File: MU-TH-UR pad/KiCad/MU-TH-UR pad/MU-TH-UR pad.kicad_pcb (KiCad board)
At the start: 2 copper layers, 186.4 x 62.5 mm, 43 parts, among them J1 OLED_DISPLAY, SW1 RotaryEncoder_Switch, SW2 SW_Push_45deg, SW3 SW_Push_45deg, SW4 SW_Push_45deg, SW5 SW_Push_45deg, U3 RP2040-Zero

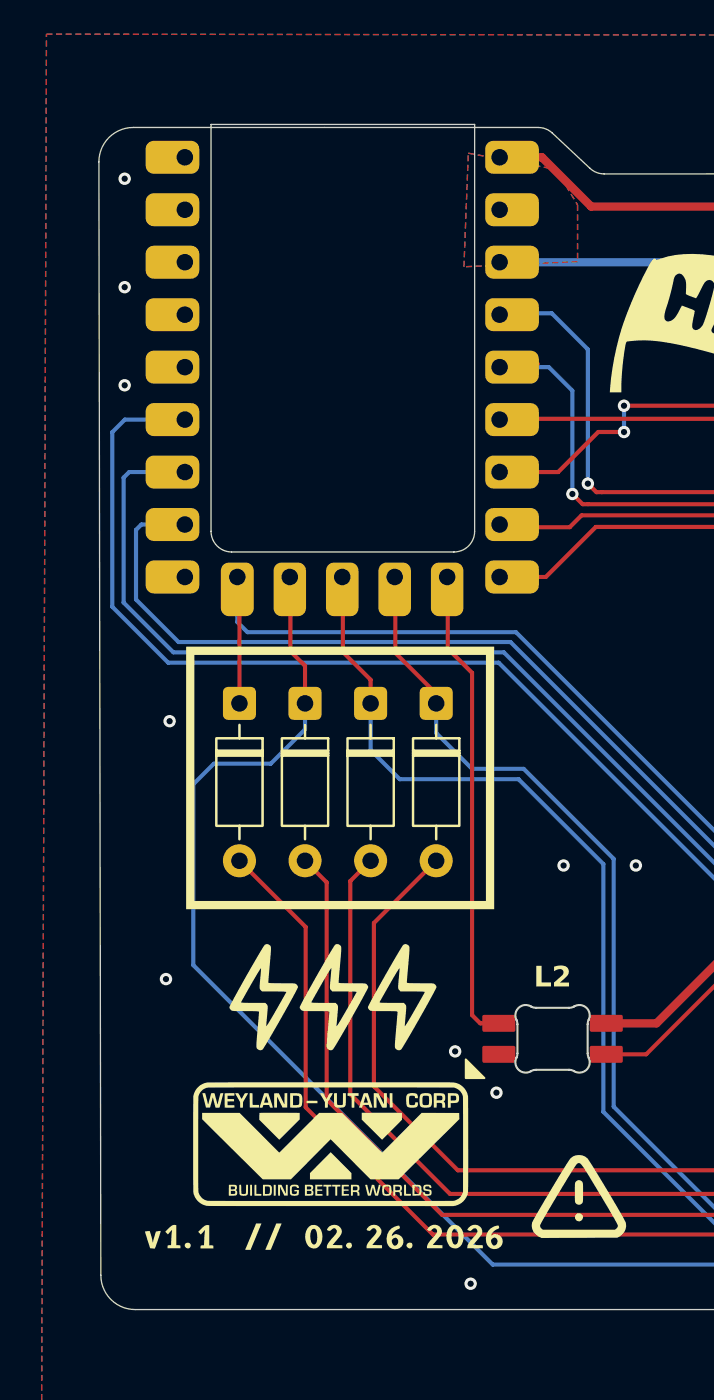
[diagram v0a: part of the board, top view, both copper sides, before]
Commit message: Fixed Edge Cut
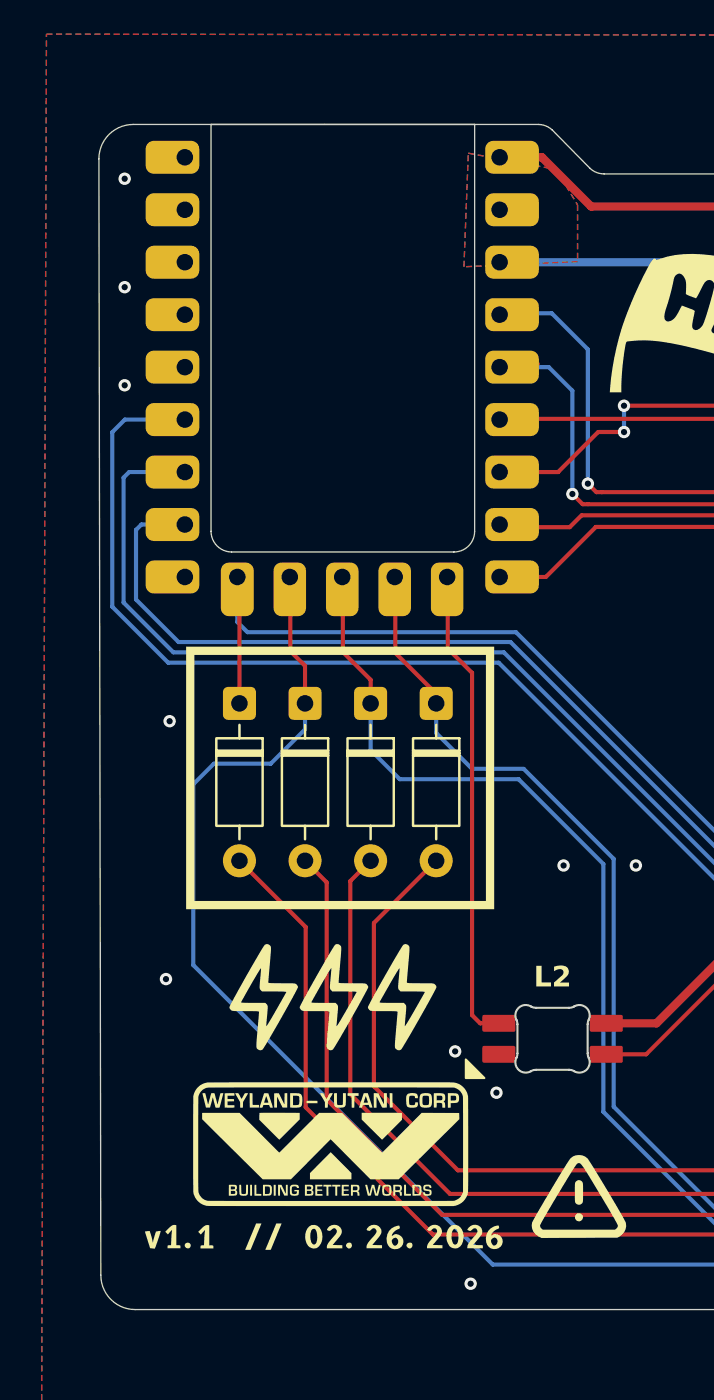
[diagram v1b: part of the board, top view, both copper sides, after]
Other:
- board size 186.4 x 62.5 mm -> 186.4 x 62.7 mm
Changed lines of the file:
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@@
 		(allow_soldermask_bridges_in_footprints no)
 		(tenting front back)
-		(grid_origin 105.626675 8.487754)
+		(grid_origin 59.631863 58.846281)
 		(pcbplotparams
 			(layerselection 0x00000000_00000000_55555555_5755f5ff)
@@
 	)
 	(gr_arc
-		(start 54.202507 60.655752)
-		(mid 54.689627 59.4797)
-		(end 55.865679 58.99258)
+		(start 54.202507 60.509453)
+		(mid 54.689627 59.333401)
+		(end 55.865679 58.846281)
 		(stroke
 			(width 0.05)
@@
 	)
 	(gr_arc
-		(start 75.470739 58.99258)
-		(mid 75.838096 59.0625)
-		(end 76.154082 59.262483)
+		(start 75.470739 58.846281)
+		(mid 75.838096 58.916201)
+		(end 76.154082 59.116184)
 		(stroke
 			(width 0.05)
@@
 	)
 	(gr_line
-		(start 76.154082 59.262483)
+		(start 76.154082 59.116213)
 		(end 77.98107 60.972474)
 		(stroke
@@
 	)
 	(gr_line
-		(start 55.865679 58.99258)
-		(end 65.115713 58.992579)
+		(start 55.865679 58.846281)
+		(end 65.115713 58.84628)
 		(stroke
 			(width 0.05)
@@
 	)
 	(gr_line
-		(start 75.470739 58.99258)
-		(end 65.115713 58.992579)
+		(start 75.470739 58.846282)
+		(end 65.115713 58.846281)
 		(stroke
 			(width 0.05)
@@
 	)
 	(gr_line
-		(start 54.202507 60.655752)
+		(start 54.202507 60.5094)
 		(end 54.296468 114.561714)
 		(stroke

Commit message: Added Serial Number Location for PCBWay
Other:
- board text added: "WayWayWay"
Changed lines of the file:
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@@
+		)
+	)
+	(gr_text "WayWayWay"
+		(at 60.881863 113.846281 0)
+		(layer "B.SilkS")
+		(effects
+			(font
+				(face "JetBrains Mono")
+				(size 1 1)
+				(thickness 0.25)
+				(bold yes)
+			)
+			(justify bottom mirror)
+		)
+		(render_cache "WayWayWay" 0
+			(polygon
+				(pts
+					(xy 64.532437 113.676281) (xy 64.638744 112.654979) (xy 64.493236 112.654979) (xy 64.428878 113.368473)
+					(xy 64.42265 113.46153) (xy 64.419109 113.557334) (xy 64.410011 113.46153) (xy 64.400913 113.368473)
+					(xy 64.311398 112.654979) (xy 64.161677 112.654979) (xy 64.077779 113.368473) (xy 64.067277 113.46153)
+					(xy 64.056774 113.557334) (xy 64.05189 113.46153) (xy 64.0456 113.368473) (xy 63.982647 112.654979)
+					(xy 63.838543 112.654979) (xy 63.950468 113.676281) (xy 64.143481 113.676281) (xy 64.221821 112.959977)
+					(xy 64.230248 112.861364) (xy 64.237209 112.765499) (xy 64.244231 112.861364) (xy 64.252657 112.959977)
+					(xy 64.337959 113.676281)
+				)
+			)
+			(polygon
+				(pts
+					(xy 63.46621 112.89735) (xy 63.525031 112.91011) (xy 63.574828 112.930177) (xy 63.617015 112.957168)
+					(xy 63.653541 112.99225) (xy 63.679792 113.031368) (xy 63.696716 113.075254) (xy 63.704393 113.125085)
+					(xy 63.536537 113.125085) (xy 63.530075 113.09812) (xy 63.51676 113.076075) (xy 63.495993 113.057919)
+					(xy 63.455506 113.040611) (xy 63.39799 113.034105) (xy 63.344983 113.039696) (xy 63.308249 113.05441)
+					(xy 63.283352 113.076786) (xy 63.267951 113.107721) (xy 63.262313 113.150242) (xy 63.262313 113.204831)
+					(xy 63.44977 113.204831) (xy 63.517072 113.209516) (xy 63.573567 113.222666) (xy 63.621071 113.243352)
+					(xy 63.66104 113.271265) (xy 63.694495 113.307049) (xy 63.718253 113.347945) (xy 63.73287 113.394972)
+					(xy 63.737976 113.449623) (xy 63.733441 113.50257) (xy 63.720459 113.548448) (xy 63.699453 113.588554)
+					(xy 63.670138 113.623829) (xy 63.634386 113.652097) (xy 63.592441 113.672718) (xy 63.543096 113.685677)
+					(xy 63.484758 113.690263) (xy 63.421602 113.685118) (xy 63.370125 113.670799) (xy 63.328076 113.648315)
+					(xy 63.293479 113.616629) (xy 63.270418 113.578439) (xy 63.2581 113.532177) (xy 63.2581 113.676281)
+					(xy 63.087436 113.676281) (xy 63.087436 113.409079) (xy 63.262313 113.409079) (xy 63.267485 113.448969)
+					(xy 63.282314 113.482003) (xy 63.307071 113.509829) (xy 63.338921 113.530071) (xy 63.378789 113.542924)
+					(xy 63.428826 113.547565) (xy 63.471557 113.54363) (xy 63.504653 113.532865) (xy 63.530248 113.516118)
+					(xy 63.549933 113.493063) (xy 63.561773 113.465742) (xy 63.565907 113.432831) (xy 63.562025 113.400686)
+					(xy 63.550865 113.37358) (xy 63.532324 113.350338) (xy 63.508141 113.332903) (xy 63.478358 113.322039)
+					(xy 63.441405 113.318159) (xy 63.262313 113.318159) (xy 63.262313 113.409079) (xy 63.087436 113.409079)
+					(xy 63.087436 113.154456) (xy 63.092956 113.093316) (xy 63.108582 113.041919) (xy 63.133664 112.998377)
+					(xy 63.168585 112.961382) (xy 63.210591 112.932813) (xy 63.261372 112.911437) (xy 63.322675 112.897729)
+					(xy 63.396647 112.892811)
+				)
+			)
+			(polygon
+				(pts
+					(xy 62.749098 113.928095) (xy 62.639922 113.634332) (xy 62.929533 112.906793) (xy 62.744885 112.906793)
+					(xy 62.596569 113.299963) (xy 62.571411 113.376167) (xy 62.553215 113.452432) (xy 62.537156 113.376167)
+					(xy 62.51261 113.299963) (xy 62.375529 112.906793) (xy 62.190881 112.906793) (xy 62.565794 113.928095)
+				)
+			)
+			(polygon
+				(pts
+					(xy 62.014782 113.676281) (xy 62.121089 112.654979) (xy 61.975581 112.654979) (xy 61.911223 113.368473)
+					(xy 61.904995 113.46153) (xy 61.901453 113.557334) (xy 61.892355 113.46153) (xy 61.883257 113.368473)
+					(xy 61.793742 112.654979) (xy 61.644021 112.654979) (xy 61.560124 113.368473) (xy 61.549622 113.46153)
+					(xy 61.539119 113.557334) (xy 61.534234 113.46153) (xy 61.527945 113.368473) (xy 61.464991 112.654979)
+					(xy 61.320888 112.654979) (xy 61.432812 113.676281) (xy 61.625825 113.676281) (xy 61.704166 112.959977)
+					(xy 61.712593 112.861364) (xy 61.719554 112.765499) (xy 61.726575 112.861364) (xy 61.735002 112.959977)
+					(xy 61.820304 113.676281)
+				)
+			)
+			(polygon
+				(pts
+					(xy 60.948555 112.89735) (xy 61.007375 112.91011) (xy 61.057173 112.930177) (xy 61.09936 112.957168)
+					(xy 61.135886 112.99225) (xy 61.162137 113.031368) (xy 61.17906 113.075254) (xy 61.186738 113.125085)
+					(xy 61.018882 113.125085) (xy 61.01242 113.09812) (xy 60.999105 113.076075) (xy 60.978338 113.057919)
+					(xy 60.937851 113.040611) (xy 60.880335 113.034105) (xy 60.827327 113.039696) (xy 60.790593 113.05441)
+					(xy 60.765697 113.076786) (xy 60.750296 113.107721) (xy 60.744658 113.150242) (xy 60.744658 113.204831)
+					(xy 60.932115 113.204831) (xy 60.999416 113.209516) (xy 61.055911 113.222666) (xy 61.103416 113.243352)
+					(xy 61.143385 113.271265) (xy 61.176839 113.307049) (xy 61.200597 113.347945) (xy 61.215214 113.394972)
+					(xy 61.220321 113.449623) (xy 61.215785 113.50257) (xy 61.202804 113.548448) (xy 61.181798 113.588554)
+					(xy 61.152483 113.623829) (xy 61.116731 113.652097) (xy 61.074786 113.672718) (xy 61.02544 113.685677)
+					(xy 60.967102 113.690263) (xy 60.903947 113.685118) (xy 60.85247 113.670799) (xy 60.810421 113.648315)
+					(xy 60.775824 113.616629) (xy 60.752763 113.578439) (xy 60.740445 113.532177) (xy 60.740445 113.676281)
+					(xy 60.56978 113.676281) (xy 60.56978 113.409079) (xy 60.744658 113.409079) (xy 60.749829 113.448969)
+					(xy 60.764659 113.482003) (xy 60.789416 113.509829) (xy 60.821266 113.530071) (xy 60.861134 113.542924)
+					(xy 60.911171 113.547565) (xy 60.953902 113.54363) (xy 60.986998 113.532865) (xy 61.012593 113.516118)
+					(xy 61.032277 113.493063) (xy 61.044118 113.465742) (xy 61.048252 113.432831) (xy 61.04437 113.400686)
+					(xy 61.033209 113.37358) (xy 61.014669 113.350338) (xy 60.990485 113.332903) (xy 60.960703 113.322039)
+					(xy 60.923749 113.318159) (xy 60.744658 113.318159) (xy 60.744658 113.409079) (xy 60.56978 113.409079)
+					(xy 60.56978 113.154456) (xy 60.5753 113.093316) (xy 60.590927 113.041919) (xy 60.616009 112.998377)
+					(xy 60.65093 112.961382) (xy 60.692936 112.932813) (xy 60.743717 112.911437) (xy 60.805019 112.897729)
+					(xy 60.878992 112.892811)
+				)
+			)
+			(polygon
+				(pts
+					(xy 60.231443 113.928095) (xy 60.122266 113.634332) (xy 60.411877 112.906793) (xy 60.22723 112.906793)
+					(xy 60.078913 113.299963) (xy 60.053756 113.376167) (xy 60.03556 113.452432) (xy 60.019501 113.376167)
+					(xy 59.994955 113.299963) (xy 59.857873 112.906793) (xy 59.673226 112.906793) (xy 60.048139 113.928095)
+				)
+			)
+			(polygon
+				(pts
+					(xy 59.497127 113.676281) (xy 59.603433 112.654979) (xy 59.457926 112.654979) (xy 59.393568 113.368473)
+					(xy 59.38734 113.46153) (xy 59.383798 113.557334) (xy 59.3747 113.46153) (xy 59.365602 113.368473)
+					(xy 59.276087 112.654979) (xy 59.126366 112.654979) (xy 59.042469 113.368473) (xy 59.031966 113.46153)
+					(xy 59.021464 113.557334) (xy 59.016579 113.46153) (xy 59.01029 113.368473) (xy 58.947336 112.654979)
+					(xy 58.803233 112.654979) (xy 58.915157 113.676281) (xy 59.10817 113.676281) (xy 59.186511 112.959977)
+					(xy 59.194937 112.861364) (xy 59.201898 112.765499) (xy 59.20892 112.861364) (xy 59.217347 112.959977)
+					(xy 59.302648 113.676281)
+				)
+			)
+			(polygon
+				(pts
+					(xy 58.4309 112.89735) (xy 58.48972 112.91011) (xy 58.539518 112.930177) (xy 58.581705 112.957168)
+					(xy 58.61823 112.99225) (xy 58.644481 113.031368) (xy 58.661405 113.075254) (xy 58.669082 113.125085)
+					(xy 58.501227 113.125085) (xy 58.494765 113.09812) (xy 58.481449 113.076075) (xy 58.460682 113.057919)
+					(xy 58.420196 113.040611) (xy 58.36268 113.034105) (xy 58.309672 113.039696) (xy 58.272938 113.05441)
+					(xy 58.248042 113.076786) (xy 58.23264 113.107721) (xy 58.227003 113.150242) (xy 58.227003 113.204831)
+					(xy 58.414459 113.204831) (xy 58.481761 113.209516) (xy 58.538256 113.222666) (xy 58.585761 113.243352)
+					(xy 58.625729 113.271265) (xy 58.659184 113.307049) (xy 58.682942 113.347945) (xy 58.697559 113.394972)
+					(xy 58.702666 113.449623) (xy 58.69813 113.50257) (xy 58.685149 113.548448) (xy 58.664142 113.588554)
+					(xy 58.634827 113.623829) (xy 58.599076 113.652097) (xy 58.557131 113.672718) (xy 58.507785 113.685677)
+					(xy 58.449447 113.690263) (xy 58.386291 113.685118) (xy 58.334815 113.670799) (xy 58.292765 113.648315)
+					(xy 58.258168 113.616629) (xy 58.235107 113.578439) (xy 58.22279 113.532177) (xy 58.22279 113.676281)
+					(xy 58.052125 113.676281) (xy 58.052125 113.409079) (xy 58.227003 113.409079) (xy 58.232174 113.448969)
+					(xy 58.247003 113.482003) (xy 58.27176 113.509829) (xy 58.303611 113.530071) (xy 58.343478 113.542924)
+					(xy 58.393515 113.547565) (xy 58.436246 113.54363) (xy 58.469342 113.532865) (xy 58.494937 113.516118)
+					(xy 58.514622 113.493063) (xy 58.526463 113.465742) (xy 58.530597 113.432831) (xy 58.526714 113.400686)
+					(xy 58.515554 113.37358) (xy 58.497013 113.350338) (xy 58.47283 113.332903) (xy 58.443047 113.322039)
+					(xy 58.406094 113.318159) (xy 58.227003 113.318159) (xy 58.227003 113.409079) (xy 58.052125 113.409079)
+					(xy 58.052125 113.154456) (xy 58.057645 113.093316) (xy 58.073272 113.041919) (xy 58.098354 112.998377)
+					(xy 58.133275 112.961382) (xy 58.17528 112.932813) (xy 58.226062 112.911437) (xy 58.287364 112.897729)
+					(xy 58.361336 112.892811)
+				)
+			)
+			(polygon
+				(pts
+					(xy 57.713788 113.928095) (xy 57.604611 113.634332) (xy 57.894222 112.906793) (xy 57.709574 112.906793)
+					(xy 57.561258 113.299963) (xy 57.536101 113.376167) (xy 57.517905 113.452432) (xy 57.501846 113.376167)
+					(xy 57.477299 113.299963) (xy 57.340218 112.906793) (xy 57.155571 112.906793) (xy 57.530483 113.928095)
+				)
+			)
 		)
 	)
